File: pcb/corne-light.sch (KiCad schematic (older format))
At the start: 92 parts, among them J1 MJ-4PP-9, J2 OLED, J6 MJ-4PP-9, J7 OLED, SW1 SW_PUSH, SW10 SW_PUSH, SW11 SW_PUSH, SW12 SW_PUSH, SW13 SW_PUSH, SW14 SW_PUSH, SW15 SW_PUSH, SW16 SW_PUSH, SW17 SW_PUSH, SW18 SW_PUSH, SW19 Rotary_Encoder_Switch, SW2 SW_PUSH, SW20 SW_PUSH, SW21 SW_PUSH, SW22 SW_PUSH, SW23 SW_PUSH, SW24 SW_PUSH, SW25 SW_PUSH, SW26 SW_PUSH, SW27 SW_PUSH, SW28 SW_PUSH, SW29 SW_PUSH, SW3 SW_PUSH, SW30 SW_PUSH, SW31 SW_PUSH, SW32 SW_PUSH, SW33 SW_PUSH, SW34 SW_PUSH, SW35 SW_PUSH, SW36 SW_PUSH, SW37 SW_PUSH, SW38 SW_PUSH, SW39 SW_PUSH, SW4 SW_PUSH, SW40 Rotary_Encoder_Switch, SW41 SW_PUSH, SW42 SW_PUSH, SW5 SW_PUSH, SW6 SW_PUSH, SW7 SW_PUSH, SW8 SW_PUSH, SW9 SW_PUSH, U1 ProMicro, U2 ProMicro

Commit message: finish alps and leds on right half
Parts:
- removed D22, D23, D24, D25, D26, D27, D28, D29, D30, D31, D32, D33, D34, D35, D36, D37, D38, D39, D40, D41, D42: D, kbd:D3_TH, symbol Device:D
- removed SW22, SW23, SW24, SW25, SW26, SW27, SW28, SW29, SW30, SW31, SW32, SW33, SW34, SW35, SW36, SW37, SW38, SW39, SW41: SW_PUSH, kbd:CherryMX_ChocV2_1u, symbol corne-light-rescue:SW_PUSH-kbd
- removed SW42: SW_PUSH, kbd:CherryMX_ChocV2_1.5u, symbol corne-light-rescue:SW_PUSH-kbd
- added D43, D44, D45, D46, D47, D48, D49, D50, D51, D52, D53, D54, D55, D56, D57, D58, D59, D60, D61, D62, D63: D_Small, Keebio-Parts:Diode-Hybrid-Back, symbol Device:D_Small
- added MX1, MX10, MX11, MX12, MX13, MX14, MX15, MX16, MX17, MX18, MX19, MX2, MX3, MX4, MX5, MX6, MX7, MX8, MX9: MX-LED, Alps_Only:ALPS-1U-LED, symbol MX_Alps_Hybrid:MX-LED
- added MX20: MX-LED, Alps_Only:ALPS-1.5U-LED, symbol MX_Alps_Hybrid:MX-LED
- added R1, R10, R11, R12, R13, R14, R15, R16, R17, R18, R19, R2, R20, R3, R4, R5, R6, R7, R8, R9: 470, Keebio-Parts:R_0805, symbol Device:R_Small
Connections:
- wire segments 124 -> 230
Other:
- moved on the sheet: J1, J2, J6, J7, RSW1, RSW2, SW40, U2

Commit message: add alps and leds to left half
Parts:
- removed D1, D10, D11, D12, D13, D14, D15, D16, D17, D18, D19, D2, D20, D21, D3, D4, D5, D6, D7, D8, D9: D, kbd:D3_TH, symbol Device:D
- removed SW1, SW10, SW11, SW12, SW13, SW14, SW15, SW16, SW17, SW18, SW2, SW20, SW3, SW4, SW5, SW6, SW7, SW8, SW9: SW_PUSH, kbd:CherryMX_ChocV2_1u, symbol corne-light-rescue:SW_PUSH-kbd
- removed SW19: Rotary_Encoder_Switch, Encoder:RollerEncoder_Panasonic_EVQWGD001, symbol Device:Rotary_Encoder_Switch
- removed SW21: SW_PUSH, kbd:CherryMX_ChocV2_1.5u, symbol corne-light-rescue:SW_PUSH-kbd
- added D1, D10, D11, D12, D13, D14, D15, D16, D17, D18, D19, D2, D20, D21, D3, D4, D5, D6, D7, D8, D9: D_Small, Keebio-Parts:Diode-Hybrid-Back, symbol Device:D_Small
- added MX21, MX22, MX23, MX24, MX25, MX26, MX27, MX28, MX29, MX30, MX31, MX32, MX33, MX34, MX35, MX36, MX37, MX38, MX39: MX-LED, Alps_Only:ALPS-1U-LED, symbol MX_Alps_Hybrid:MX-LED
- added MX40: MX-LED, Alps_Only:ALPS-1.5U-LED, symbol MX_Alps_Hybrid:MX-LED
- added Q1, Q2: Q_NPN_BEC, Package_TO_SOT_SMD:SOT-23, symbol Device:Q_NPN_BEC
- added R21, R22: 1k, Keebio-Parts:R_0805, symbol Device:R_Small
- added R23, R24, R25, R26, R27, R28, R29, R30, R31, R32, R33, R34, R35, R36, R37, R38, R39, R40, R41, R42: 470, Keebio-Parts:R_0805, symbol Device:R_Small
- added SW1: Rotary_Encoder_Switch, Encoder:RollerEncoder_Panasonic_EVQWGD001, symbol Device:Rotary_Encoder_Switch
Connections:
- net labels added: PWM, PWM_r
- wire segments 230 -> 344
- no-connect marks 11 -> 10
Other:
- moved on the sheet: D43, D44, D45, D46, D47, D48, D49, D50, D51, D52, D53, D54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

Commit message: Finish RGB
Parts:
- added LED1, LED10, LED2, LED3, LED4, LED5, LED6, LED7, LED8, LED9: YS-SK6812MINI-E, Keebio-Parts:SK6812-MINI-E, symbol kbd:YS-SK6812MINI-E
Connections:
- net labels added: DIN, DIN_r
- wire segments 344 -> 375

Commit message: Remove RGB and add a new image
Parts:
- removed LED1, LED10, LED2, LED3, LED4, LED5, LED6, LED7, LED8, LED9: YS-SK6812MINI-E, Keebio-Parts:SK6812-MINI-E, symbol kbd:YS-SK6812MINI-E
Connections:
- wire segments 375 -> 344
- no-connect marks 10 -> 8
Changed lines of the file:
@@
 Wire Wire Line
 	6310 2030 6310 2075
-$Comp
-L kbd:YS-SK6812MINI-E LED1
-U 1 1 60A20866
-P 1255 6470
-F 0 "LED1" H 1599 6500 29  0000 L CNN
-F 1 "YS-SK6812MINI-E" H 1599 6441 29  0000 L CNN
-F 2 "Keebio-Parts:SK6812-MINI-E" H 1355 6220 50  0001 C CNN
-F 3 "" H 1355 6220 50  0001 C CNN
-	1    1255 6470
-	1    0    0    -1
-$EndComp
-Text GLabel 955  6470 0    50   Input ~ 0
-DIN_r
 Text GLabel 1050 725  0    50   Input ~ 0
 DIN_r
-$Comp
-L kbd:YS-SK6812MINI-E LED2
-U 1 1 60A76638
-P 2225 6470
-F 0 "LED2" H 2569 6500 29  0000 L CNN
-F 1 "YS-SK6812MINI-E" H 2569 6441 29  0000 L CNN
-F 2 "Keebio-Parts:SK6812-MINI-E" H 2325 6220 50  0001 C CNN
-F 3 "" H 2325 6220 50  0001 C CNN
-	1    2225 6470
-	1    0    0    -1
-$EndComp
-Wire Wire Line
-	1555 6470 1925 6470
-$Comp
-L kbd:YS-SK6812MINI-E LED3
-U 1 1 60A95241
-P 3195 6470
-F 0 "LED3" H 3539 6500 29  0000 L CNN
-F 1 "YS-SK6812MINI-E" H 3539 6441 29  0000 L CNN
-F 2 "Keebio-Parts:SK6812-MINI-E" H 3295 6220 50  0001 C CNN
-F 3 "" H 3295 6220 50  0001 C CNN
-	1    3195 6470
-	1    0    0    -1
-$EndComp
-Wire Wire Line
-	2895 6470 2525 6470
-$Comp
-L kbd:YS-SK6812MINI-E LED4
-U 1 1 60AB3FC0
-P 4165 6470
-F 0 "LED4" H 4509 6500 29  0000 L CNN
-F 1 "YS-SK6812MINI-E" H 4509 6441 29  0000 L CNN
-F 2 "Keebio-Parts:SK6812-MINI-E" H 4265 6220 50  0001 C CNN
-F 3 "" H 4265 6220 50  0001 C CNN
-	1    4165 6470
-	1    0    0    -1
-$EndComp
-Wire Wire Line
-	3495 6470 3865 6470
-$Comp
-L kbd:YS-SK6812MINI-E LED5
-U 1 1 60ADAEBF
-P 5140 6470
-F 0 "LED5" H 5484 6500 29  0000 L CNN
-F 1 "YS-SK6812MINI-E" H 5484 6441 29  0000 L CNN
-F 2 "Keebio-Parts:SK6812-MINI-E" H 5240 6220 50  0001 C CNN
-F 3 "" H 5240 6220 50  0001 C CNN
-	1    5140 6470
-	1    0    0    -1
-$EndComp
-Wire Wire Line
-	4465 6470 4840 6470
-Wire Wire Line
-	1255 6770 2225 6770
-Wire Wire Line
-	5455 6770 5455 6905
-Connection ~ 2225 6770
-Wire Wire Line
-	2225 6770 3195 6770
-Connection ~ 3195 6770
-Wire Wire Line
-	3195 6770 4165 6770
-Connection ~ 4165 6770
-Wire Wire Line
-	4165 6770 5140 6770
-Connection ~ 5140 6770
-Wire Wire Line
-	5140 6770 5455 6770
-$Comp
-L power:GNDA #PWR0123
-U 1 1 60B1BE65
-P 5455 6905
-F 0 "#PWR0123" H 5455 6655 50  0001 C CNN
-F 1 "GNDA" V 5370 6880 50  0000 C CNN
-F 2 "" H 5455 6905 50  0001 C CNN
-F 3 "" H 5455 6905 50  0001 C CNN
-	1    5455 6905
-	1    0    0    -1
-$EndComp
-Wire Wire Line
-	1255 6170 2225 6170
-Connection ~ 2225 6170
-Wire Wire Line
-	2225 6170 3195 6170
-Connection ~ 3195 6170
-Wire Wire Line
-	3195 6170 4165 6170
-Connection ~ 4165 6170
-Wire Wire Line
-	4165 6170 5140 6170
-Connection ~ 5140 6170
-Wire Wire Line
-	5140 6170 5435 6170
-Wire Wire Line
-	5435 6055 5435 6170
-$Comp
-L power:VDD #PWR0124
-U 1 1 60B6BC99
-P 5435 6055
-F 0 "#PWR0124" H 5435 5905 50  0001 C CNN
-F 1 "VDD" H 5450 6228 50  0000 C CNN
-F 2 "" H 5435 6055 50  0001 C CNN
-F 3 "" H 5435 6055 50  0001 C CNN
-	1    5435 6055
-	1    0    0    -1
-$EndComp
-NoConn ~ 5440 6470
-$Comp
-L kbd:YS-SK6812MINI-E LED6
-U 1 1 60D1A40D
-P 1435 7365
-F 0 "LED6" H 1779 7395 29  0000 L CNN
-F 1 "YS-SK6812MINI-E" H 1779 7336 29  0000 L CNN
-F 2 "Keebio-Parts:SK6812-MINI-E" H 1535 7115 50  0001 C CNN
-F 3 "" H 1535 7115 50  0001 C CNN
-	1    1435 7365
-	1    0    0    -1
-$EndComp
-$Comp
-L kbd:YS-SK6812MINI-E LED7
-U 1 1 60D1AC5C
-P 2405 7365
-F 0 "LED7" H 2749 7395 29  0000 L CNN
-F 1 "YS-SK6812MINI-E" H 2749 7336 29  0000 L CNN
-F 2 "Keebio-Parts:SK6812-MINI-E" H 2505 7115 50  0001 C CNN
-F 3 "" H 2505 7115 50  0001 C CNN
-	1    2405 7365
-	1    0    0    -1
-$EndComp
-Wire Wire Line
-	1735 7365 2105 7365
-$Comp
-L kbd:YS-SK6812MINI-E LED8
-U 1 1 60D1AC67
-P 3375 7365
-F 0 "LED8" H 3719 7395 29  0000 L CNN
-F 1 "YS-SK6812MINI-E" H 3719 7336 29  0000 L CNN
-F 2 "Keebio-Parts:SK6812-MINI-E" H 3475 7115 50  0001 C CNN
-F 3 "" H 3475 7115 50  0001 C CNN
-	1    3375 7365
-	1    0    0    -1
-$EndComp
-Wire Wire Line
-	3075 7365 2705 7365
-$Comp
-L kbd:YS-SK6812MINI-E LED9
-U 1 1 60D1AC72
-P 4345 7365
-F 0 "LED9" H 4689 7395 29  0000 L CNN
-F 1 "YS-SK6812MINI-E" H 4689 7336 29  0000 L CNN
-F 2 "Keebio-Parts:SK6812-MINI-E" H 4445 7115 50  0001 C CNN
-F 3 "" H 4445 7115 50  0001 C CNN
-	1    4345 7365
-	1    0    0    -1
-$EndComp
-Wire Wire Line
-	3675 7365 4045 7365
-$Comp
-L kbd:YS-SK6812MINI-E LED10
-U 1 1 60D1AC7D
-P 5320 7365
-F 0 "LED10" H 5664 7395 29  0000 L CNN
-F 1 "YS-SK6812MINI-E" H 5664 7336 29  0000 L CNN
-F 2 "Keebio-Parts:SK6812-MINI-E" H 5420 7115 50  0001 C CNN
-F 3 "" H 5420 7115 50  0001 C CNN
-	1    5320 7365
-	1    0    0    -1
-$EndComp
-Wire Wire Line
-	4645 7365 5020 7365
-Wire Wire Line
-	1435 7665 2405 7665
-Connection ~ 2405 7665
-Wire Wire Line
-	2405 7665 3375 7665
-Connection ~ 3375 7665
-Wire Wire Line
-	3375 7665 4345 7665
-Connection ~ 4345 7665
-Wire Wire Line
-	4345 7665 5320 7665
-Connection ~ 5320 7665
-Wire Wire Line
-	5320 7665 5635 7665
-Wire Wire Line
-	1435 7065 2405 7065
-Connection ~ 2405 7065
-Wire Wire Line
-	2405 7065 3375 7065
-Connection ~ 3375 7065
-Wire Wire Line
-	3375 7065 4345 7065
-Connection ~ 4345 7065
-Wire Wire Line
-	4345 7065 5320 7065
-Connection ~ 5320 7065
-Wire Wire Line
-	5320 7065 5615 7065
-Wire Wire Line
-	5615 6950 5615 7065
-NoConn ~ 5620 7365
-$Comp
-L power:GND #PWR0125
-U 1 1 60F0672D
-P 5635 7665
-F 0 "#PWR0125" H 5635 7415 50  0001 C CNN
-F 1 "GND" H 5630 7705 50  0000 C CNN
-F 2 "" H 5635 7665 50  0001 C CNN
-F 3 "" H 5635 7665 50  0001 C CNN
-	1    5635 7665
-	1    0    0    -1
-$EndComp
-$Comp
-L power:VCC #PWR0126
-U 1 1 60F2D365
-P 5615 6950
-F 0 "#PWR0126" H 5615 6800 50  0001 C CNN
-F 1 "VCC" H 5630 7123 50  0000 C CNN
-F 2 "" H 5615 6950 50  0001 C CNN
-F 3 "" H 5615 6950 50  0001 C CNN
-	1    5615 6950
-	1    0    0    -1
-$EndComp
-Text GLabel 1135 7365 0    50   Input ~ 0
-DIN
 Text GLabel 4145 730  0    50   Input ~ 0
 DIN

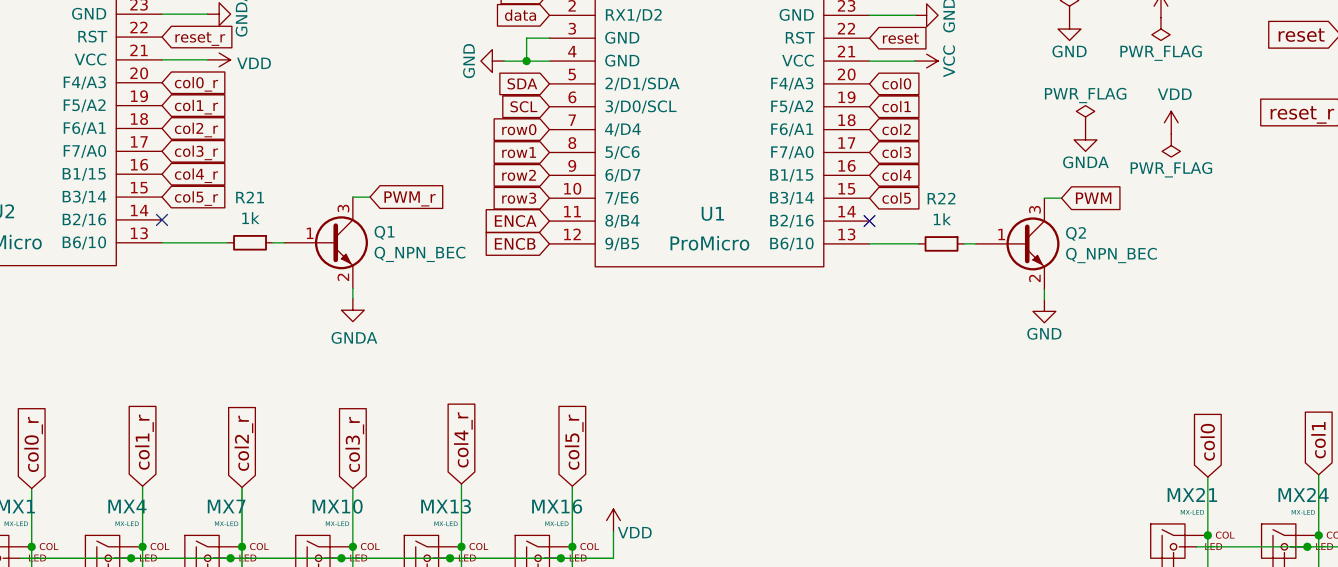
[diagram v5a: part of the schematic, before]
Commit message: Fix mosfet and add add silkscreen stuff
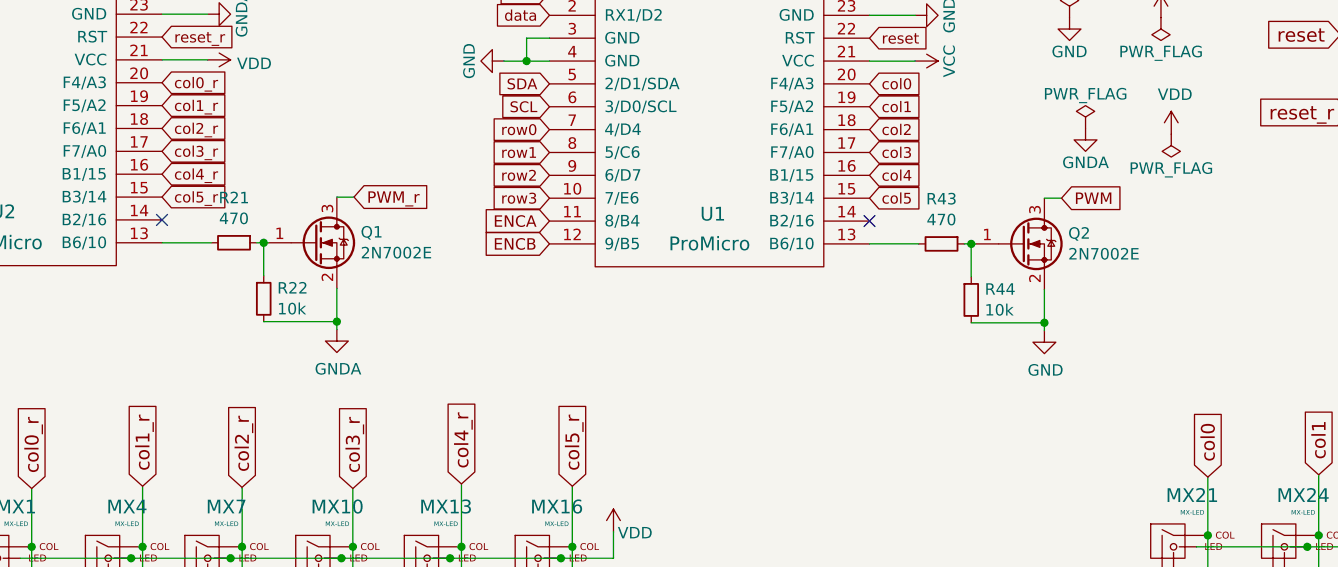
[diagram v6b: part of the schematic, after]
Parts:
- removed Q1, Q2: Q_NPN_BEC, Package_TO_SOT_SMD:SOT-23, symbol Device:Q_NPN_BEC
- added Q1, Q2: 2N7002E, Package_TO_SOT_SMD:SOT-23, symbol Transistor_FET:2N7002E
- added R43: 470, Keebio-Parts:R_0805, symbol Device:R_Small
- added R44: 10k, Keebio-Parts:R_0805, symbol Device:R_Small
- D1: footprint Keebio-Parts:Diode-Hybrid-Back -> Keebio-Parts:Diode-hybrid-3pad
- R21: value 1k -> 470
- R22: value 1k -> 10k
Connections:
- net GND: now also Q2.2 (S), R44.2
- net GNDA: now also R22.2, Q1.2 (S)
- net PWM: now also Q2.3 (D)
- net PWM_r: now also Q1.3 (D)
- net at U1.13 (B6/10): now also R43.2; no longer R22.2
- net at R21.1: now also R22.1, Q1.1 (G)
- new net: Q2.1 (G), R43.1, R44.1
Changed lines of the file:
@@
 F 0 "D1" H 6900 3725 50  0000 R CNN
 F 1 "D_Small" H 7005 3645 50  0000 R CNN
-F 2 "Keebio-Parts:Diode-Hybrid-Back" V 6825 3545 50  0001 C CNN
+F 2 "Keebio-Parts:Diode-hybrid-3pad" V 6825 3545 50  0001 C CNN
 F 3 "~" V 6825 3545 50  0001 C CNN
 	1    6825 3545
@@
 Text GLabel 7510 2840 1    60   Input ~ 0
 col1
-Wire Wire Line
-	3285 1625 3360 1625
-Text GLabel 3360 1625 2    50   Input ~ 0
-PWM_r
-Wire Wire Line
-	2935 1825 2985 1825
-$Comp
-L Device:R_Small R21
-U 1 1 60ADB37B
-P 2835 1825
-F 0 "R21" V 2639 1825 50  0000 C CNN
-F 1 "1k" V 2730 1825 50  0000 C CNN
-F 2 "Keebio-Parts:R_0805" H 2835 1825 50  0001 C CNN
-F 3 "~" H 2835 1825 50  0001 C CNN
-	1    2835 1825
-	0    1    1    0
-$EndComp
-$Comp
-L Device:Q_NPN_BEC Q1
-U 1 1 60A1EE59
-P 3185 1825
-F 0 "Q1" H 3376 1871 50  0000 L CNN
-F 1 "Q_NPN_BEC" H 3376 1780 50  0000 L CNN
-F 2 "Package_TO_SOT_SMD:SOT-23" H 3385 1925 50  0001 C CNN
-F 3 "~" H 3185 1825 50  0001 C CNN
-	1    3185 1825
-	1    0    0    -1
-$EndComp
-Wire Wire Line
-	2450 1825 2735 1825
-$Comp
-L power:GNDA #PWR0112
-U 1 1 60A4E817
-P 3285 2070
-F 0 "#PWR0112" H 3285 1820 50  0001 C CNN
-F 1 "GNDA" H 3290 1897 50  0000 C CNN
-F 2 "" H 3285 2070 50  0001 C CNN
-F 3 "" H 3285 2070 50  0001 C CNN
-	1    3285 2070
-	1    0    0    -1
-$EndComp
-Wire Wire Line
-	3285 2025 3285 2070
 Text GLabel 2450 1625 2    47   Input ~ 0
 col5_r
@@
 NoConn ~ -2045 5365
 Wire Wire Line
-	5960 1830 6010 1830
-$Comp
-L Device:R_Small R22
-U 1 1 618DCBE6
+	5545 1830 5760 1830
+Wire Wire Line
+	6310 1630 6385 1630
+Text GLabel 6385 1630 2    50   Input ~ 0
+PWM
+Text GLabel 1050 725  0    50   Input ~ 0
+DIN_r
+Text GLabel 4145 730  0    50   Input ~ 0
+DIN
+$Comp
+L Transistor_FET:2N7002E Q2
+U 1 1 60A6FC42
+P 6210 1830
+F 0 "Q2" H 6414 1876 50  0000 L CNN
+F 1 "2N7002E" H 6414 1785 50  0000 L CNN
+F 2 "Package_TO_SOT_SMD:SOT-23" H 6410 1755 50  0001 L CIN
+F 3 "http://www.diodes.com/assets/Datasheets/ds30376.pdf" H 6210 1830 50  0001 L CNN
+	1    6210 1830
+	1    0    0    -1
+$EndComp
+$Comp
+L Device:R_Small R43
+U 1 1 60B32049
 P 5860 1830
-F 0 "R22" V 5664 1830 50  0000 C CNN
-F 1 "1k" V 5755 1830 50  0000 C CNN
+F 0 "R43" V 5664 1830 50  0000 C CNN
+F 1 "470" V 5755 1830 50  0000 C CNN
 F 2 "Keebio-Parts:R_0805" H 5860 1830 50  0001 C CNN
 F 3 "~" H 5860 1830 50  0001 C CNN
@@
 	0    1    1    0
 $EndComp
-$Comp
-L Device:Q_NPN_BEC Q2
-U 1 1 618DCBF0
-P 6210 1830
-F 0 "Q2" H 6401 1876 50  0000 L CNN
-F 1 "Q_NPN_BEC" H 6401 1785 50  0000 L CNN
-F 2 "Package_TO_SOT_SMD:SOT-23" H 6410 1930 50  0001 C CNN
-F 3 "~" H 6210 1830 50  0001 C CNN
-	1    6210 1830
-	1    0    0    -1
-$EndComp
-Wire Wire Line
-	5545 1830 5760 1830
-Wire Wire Line
-	6310 1630 6385 1630
-Text GLabel 6385 1630 2    50   Input ~ 0
-PWM
+Wire Wire Line
+	5960 1830 5990 1830
+$Comp
+L Device:R_Small R44
+U 1 1 60B544DB
+P 5990 2075
+F 0 "R44" H 6049 2121 50  0000 L CNN
+F 1 "10k" H 6049 2030 50  0000 L CNN
+F 2 "Keebio-Parts:R_0805" H 5990 2075 50  0001 C CNN
+F 3 "~" H 5990 2075 50  0001 C CNN
+	1    5990 2075
+	1    0    0    -1
+$EndComp
+Wire Wire Line
+	5990 1975 5990 1830
+Connection ~ 5990 1830
+Wire Wire Line
+	5990 1830 6010 1830
+Wire Wire Line
+	6310 2030 6310 2175
 $Comp
 L power:GND #PWR0122
-U 1 1 61A16525
-P 6310 2075
-F 0 "#PWR0122" H 6310 1825 50  0001 C CNN
-F 1 "GND" H 6310 1925 50  0000 C CNN
-F 2 "" H 6310 2075 50  0001 C CNN
-F 3 "" H 6310 2075 50  0001 C CNN
-	1    6310 2075
-	1    0    0    -1
-$EndComp
-Wire Wire Line
-	6310 2030 6310 2075
-Text GLabel 1050 725  0    50   Input ~ 0
-DIN_r
-Text GLabel 4145 730  0    50   Input ~ 0
-DIN
+U 1 1 60BB122F
+P 6310 2210
+F 0 "#PWR0122" H 6310 1960 50  0001 C CNN
+F 1 "GND" H 6315 2037 50  0000 C CNN
+F 2 "" H 6310 2210 50  0001 C CNN
+F 3 "" H 6310 2210 50  0001 C CNN
+	1    6310 2210
+	1    0    0    -1
+$EndComp
+Wire Wire Line
+	5990 2175 6310 2175
+Connection ~ 6310 2175
+Wire Wire Line
+	6310 2175 6310 2210
+Wire Wire Line
+	2450 1825 2665 1825
+Wire Wire Line
+	3215 1625 3290 1625
+$Comp
+L Transistor_FET:2N7002E Q1
+U 1 1 60C25ED5
+P 3115 1825
+F 0 "Q1" H 3319 1871 50  0000 L CNN
+F 1 "2N7002E" H 3319 1780 50  0000 L CNN
+F 2 "Package_TO_SOT_SMD:SOT-23" H 3315 1750 50  0001 L CIN
+F 3 "http://www.diodes.com/assets/Datasheets/ds30376.pdf" H 3115 1825 50  0001 L CNN
+	1    3115 1825
+	1    0    0    -1
+$EndComp
+$Comp
+L Device:R_Small R21
+U 1 1 60C25EDF
+P 2765 1825
+F 0 "R21" V 2569 1825 50  0000 C CNN
+F 1 "470" V 2660 1825 50  0000 C CNN
+F 2 "Keebio-Parts:R_0805" H 2765 1825 50  0001 C CNN
+F 3 "~" H 2765 1825 50  0001 C CNN
+	1    2765 1825
+	0    1    1    0
+$EndComp
+Wire Wire Line
+	2865 1825 2895 1825
+$Comp
+L Device:R_Small R22
+U 1 1 60C25EEA
+P 2895 2070
+F 0 "R22" H 2954 2116 50  0000 L CNN
+F 1 "10k" H 2954 2025 50  0000 L CNN
+F 2 "Keebio-Parts:R_0805" H 2895 2070 50  0001 C CNN
+F 3 "~" H 2895 2070 50  0001 C CNN
+	1    2895 2070
+	1    0    0    -1
+$EndComp
+Wire Wire Line
+	2895 1970 2895 1825
+Connection ~ 2895 1825
+Wire Wire Line
+	2895 1825 2915 1825
+Wire Wire Line
+	3215 2025 3215 2170
+Wire Wire Line
+	2895 2170 3215 2170
+Connection ~ 3215 2170
+Wire Wire Line
+	3215 2170 3215 2205
+Text GLabel 3290 1625 2    50   Input ~ 0
+PWM_r
+$Comp
+L power:GNDA #PWR?
+U 1 1 60E4B44B
+P 3215 2205
+F 0 "#PWR?" H 3215 1955 50  0001 C CNN
+F 1 "GNDA" H 3220 2032 50  0000 C CNN
+F 2 "" H 3215 2205 50  0001 C CNN
+F 3 "" H 3215 2205 50  0001 C CNN
+	1    3215 2205
+	1    0    0    -1
+$EndComp
 $EndSCHEMATC

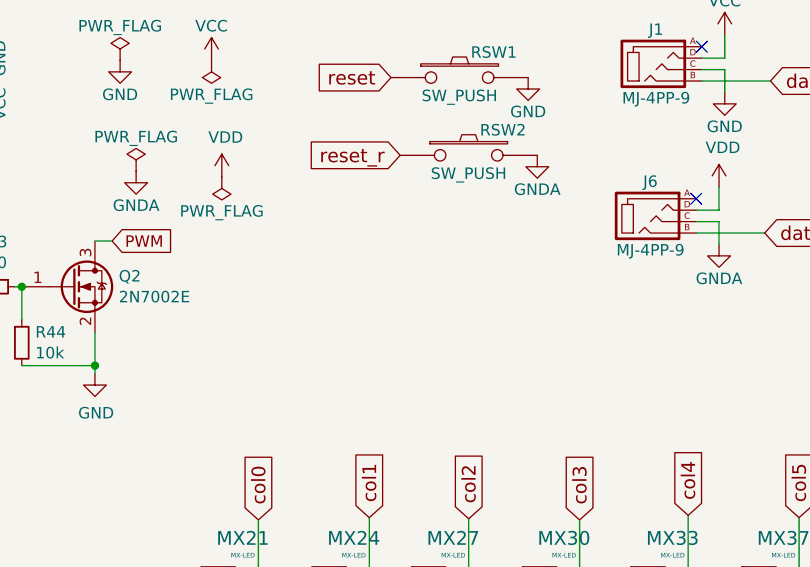
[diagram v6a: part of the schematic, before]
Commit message: Add trackball support
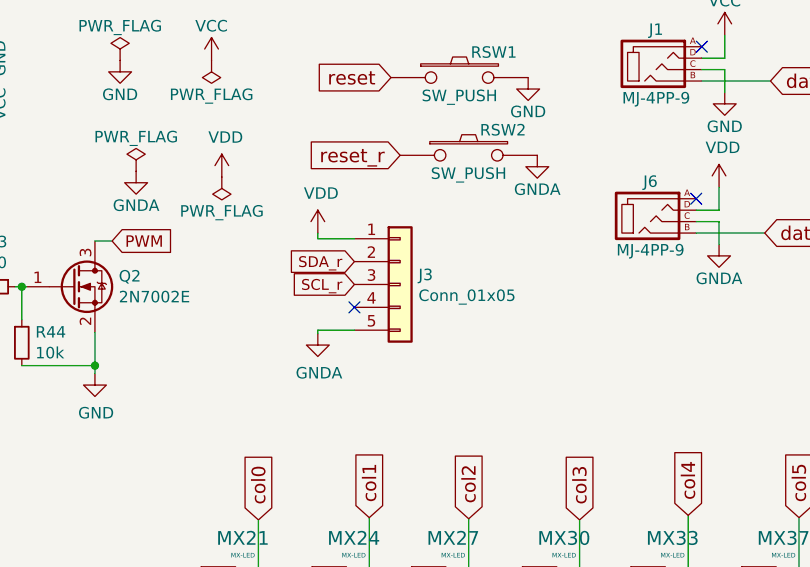
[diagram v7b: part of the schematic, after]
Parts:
- added J3: Conn_01x05, other_parts:pimoroni_left_side_mount, symbol Connector_Generic:Conn_01x05
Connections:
- net GNDA: now also J3.5 (Pin_5)
- net SCL_r: now also J3.3 (Pin_3)
- net SDA_r: now also J3.2 (Pin_2)
- net VDD: now also J3.1 (Pin_1)
- no-connect marks 8 -> 9
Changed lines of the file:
@@
 PWM_r
 $Comp
-L power:GNDA #PWR?
+L power:GNDA #PWR0112
 U 1 1 60E4B44B
 P 3215 2205
-F 0 "#PWR?" H 3215 1955 50  0001 C CNN
+F 0 "#PWR0112" H 3215 1955 50  0001 C CNN
 F 1 "GNDA" H 3220 2032 50  0000 C CNN
 F 2 "" H 3215 2205 50  0001 C CNN
@@
 	1    0    0    -1
 $EndComp
+$Comp
+L Connector_Generic:Conn_01x05 J3
+U 1 1 60B0CB12
+P 7645 1820
+F 0 "J3" H 7725 1862 50  0000 L CNN
+F 1 "Conn_01x05" H 7725 1771 50  0000 L CNN
+F 2 "other_parts:pimoroni_left_side_mount" H 7645 1820 50  0001 C CNN
+F 3 "~" H 7645 1820 50  0001 C CNN
+	1    7645 1820
+	1    0    0    -1
+$EndComp
+$Comp
+L power:VDD #PWR0123
+U 1 1 60B297C6
+P 7285 1595
+F 0 "#PWR0123" H 7285 1445 50  0001 C CNN
+F 1 "VDD" H 7300 1768 50  0000 C CNN
+F 2 "" H 7285 1595 50  0001 C CNN
+F 3 "" H 7285 1595 50  0001 C CNN
+	1    7285 1595
+	1    0    0    -1
+$EndComp
+Wire Wire Line
+	7445 1620 7285 1620
+Wire Wire Line
+	7285 1620 7285 1595
+Text GLabel 7445 1720 0    47   Input ~ 0
+SDA_r
+Text GLabel 7445 1820 0    47   Input ~ 0
+SCL_r
+NoConn ~ 7445 1920
+Wire Wire Line
+	7445 2020 7285 2020
+Wire Wire Line
+	7285 2020 7285 2035
+$Comp
+L power:GNDA #PWR0124
+U 1 1 60C362F8
+P 7285 2035
+F 0 "#PWR0124" H 7285 1785 50  0001 C CNN
+F 1 "GNDA" H 7290 1862 50  0000 C CNN
+F 2 "" H 7285 2035 50  0001 C CNN
+F 3 "" H 7285 2035 50  0001 C CNN
+	1    7285 2035
+	1    0    0    -1
+$EndComp
